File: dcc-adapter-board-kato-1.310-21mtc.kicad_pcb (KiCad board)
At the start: 2 copper layers, 59.5 x 16 mm, 25 parts

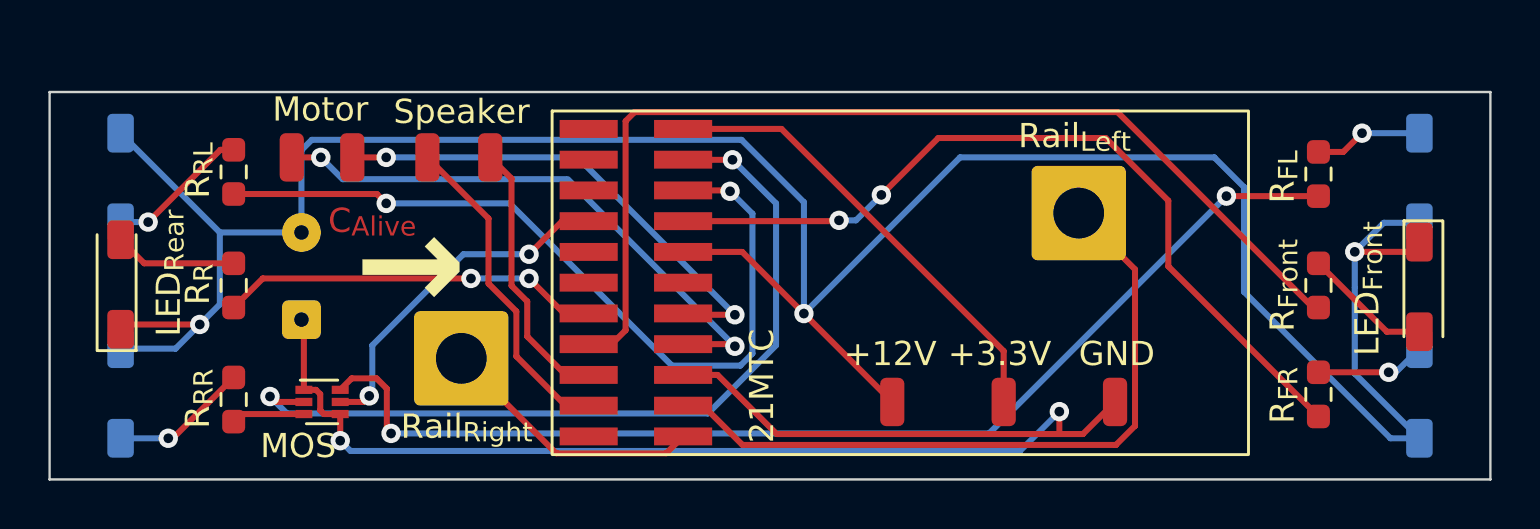
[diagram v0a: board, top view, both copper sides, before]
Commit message: 試作1号　フィードバック
ねじ穴位置修正
プラス表記
銅層の文字をシルクスクリーンに移動
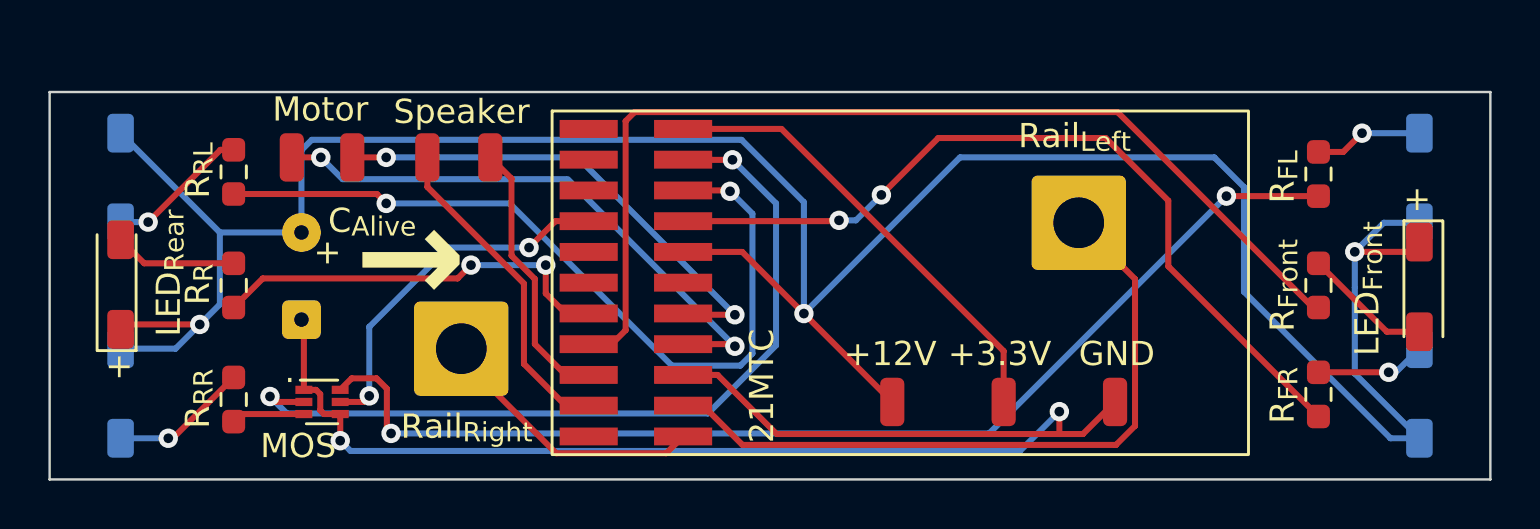
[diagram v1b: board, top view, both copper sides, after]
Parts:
- moved Rail_{Left}1 0.40 mm to (106.0, 30.8)
- moved Rail_{Right}1 0.40 mm to (80.5, 36.0)
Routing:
- net Net-(21MTC1-Rearlight): track 15.8 -> 16.9 mm
- net Net-(21MTC1-Aux_4): track 14.5 -> 15.0 mm
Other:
- board text added: "+"
- board text added: "."

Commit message: 改修
• 21MTC のピン配置がまちがっていた
• アライブキャパシター用端子をなくした
  • +12V・GND パッドを使うようにする
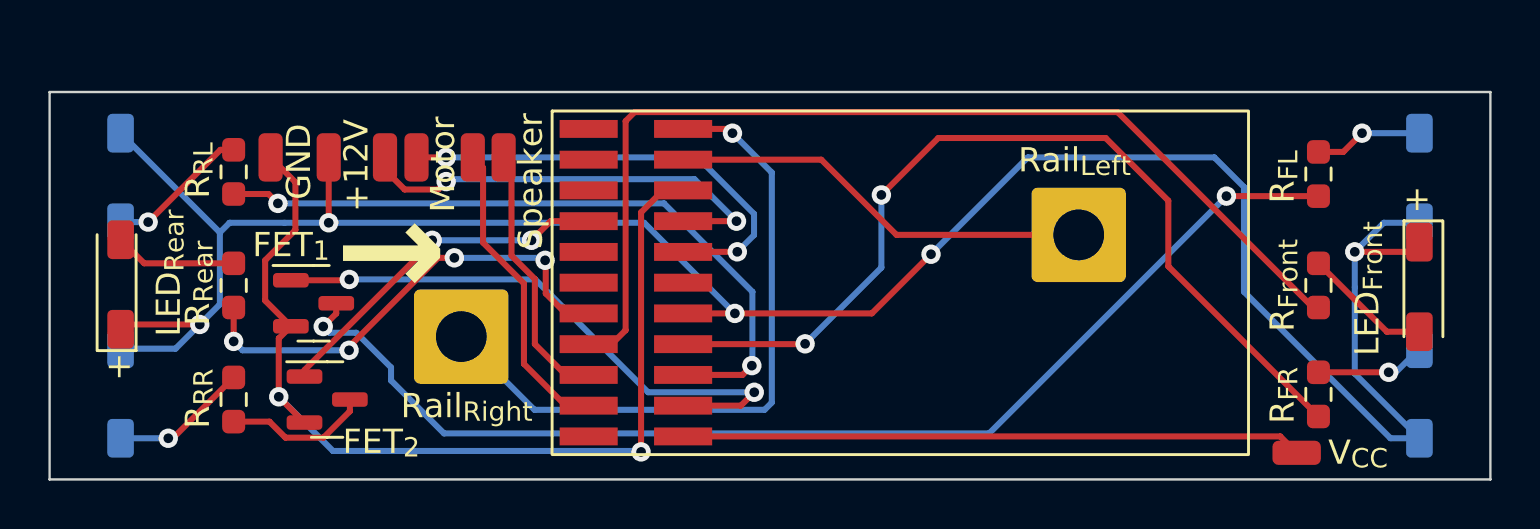
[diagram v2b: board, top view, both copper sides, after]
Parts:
- removed +3.3V1: J, Connector_Wire:SolderWirePad_1x01_SMD_1x2mm
- removed C_{Alive}1: C, Connector_Wire:SolderWire-0.1sqmm_1x02_P3.6mm_D0.4mm_OD1mm
- removed MOS1: NMOS, Package_TO_SOT_SMD:SOT-563
- added Q1: NMOSFET1, Package_TO_SOT_SMD:SOT-23, F.Cu at (74.4, 34.1)
- added Q2: NMOSFET2, Package_TO_SOT_SMD:SOT-23, F.Cu at (75.0, 38.1)
- added VCC1: J, Connector_Wire:SolderWirePad_1x01_SMD_1x2mm, F.Cu at (115.0, 40.3)
- moved GND1 36.3 mm to (72.6, 28.1)
- moved +12V1 25.4 mm to (75.0, 28.1)
- moved G1 8.26 mm to (87.6, 29.9)
- moved Motor_{1}1 3.85 mm to (77.3, 28.1)
- moved Motor_{2}1 2.65 mm to (78.7, 28.1)
- moved Speaker_{1}1 1.88 mm to (81.0, 28.1)
- moved Speaker_{2}1 0.55 mm to (82.2, 28.1)
- moved Rail_{Left}1 0.50 mm to (106.0, 31.3)
- moved Rail_{Right}1 0.50 mm to (80.5, 35.5)
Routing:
- net Net-(21MTC1-Rail_Right): track 11.5 -> 28.1 mm, vias 0 -> 1
- net GND: track 57.2 -> 40.9 mm
- net +12V: track 111.8 -> 97.9 mm, vias 3 -> 5
- net Net-(21MTC1-Rail_Left): track 29.0 -> 17.6 mm
- net Net-(21MTC1-Aux_3): track 34.3 -> 24.2 mm
- net Net-(21MTC1-Vcc): track 19.1 -> 25.6 mm
- net Net-(21MTC1-Motor_1): track 23.6 -> 18.5 mm
- net Net-(21MTC1-Aux_2): track 33.6 -> 29.2 mm
- net Net-(21MTC1-Aux_1): track 34.0 -> 37.9 mm
- net Net-(Q2-D): track 3.03 -> 6.01 mm
- net Net-(21MTC1-Rearlight): track 16.9 -> 19.6 mm, vias 2 -> 4
- net Net-(Q1-D): track 46.6 -> 48.5 mm
- net Net-(21MTC1-Motor_2): track 20.7 -> 19.0 mm
- net Net-(Speaker_{1}1-Pin_1): track 13.6 -> 12.8 mm
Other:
- board text added: "FET_{1}"
- board text added: "FET_{2}"
- board text added: "K 1-310 21MTC Adaptor Board ver. 2 2023.05.18 岡本和樹"
- board text added: "R_{Rear}"
- board text added: "V_{CC}"
- board text removed: "+3.3V"
- board text removed: "."
- board text removed: "21MTC"
- board text removed: "C_{Alive}"
- board text removed: "K 1-310 21MTC Adaptor Board ver. 1 2023.04.17 岡本和樹"
- board text removed: "MOS"
- board text removed: "R_{R}"

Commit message: v2 フィードバック
• MOSFET のゲートの前段に抵抗を追加
• ねじ穴の位置を 0.5mm 外側に移動
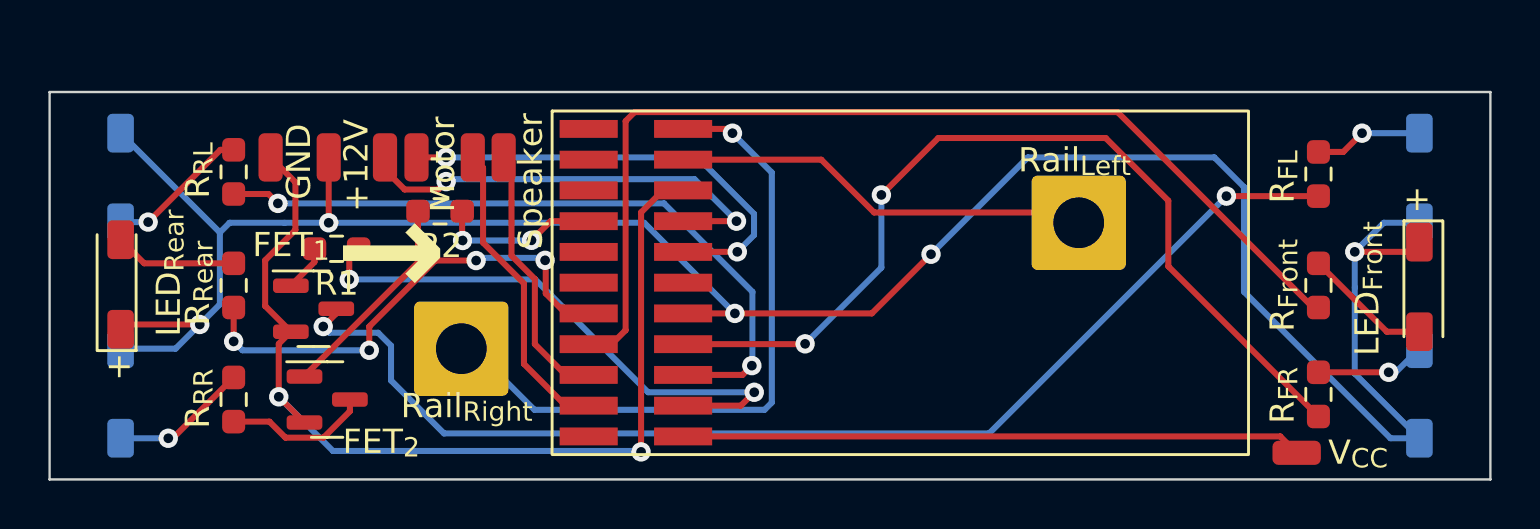
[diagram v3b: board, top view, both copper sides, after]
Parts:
- added R1: 1kΩ, Resistor_SMD:R_0603_1608Metric_Pad0.98x0.95mm_HandSolder, F.Cu at (75.3, 31.9)
- added R2: 1kΩ, Resistor_SMD:R_0603_1608Metric_Pad0.98x0.95mm_HandSolder, F.Cu at (79.6, 30.3)
- moved Rail_{Left}1 0.50 mm to (106.0, 30.8)
- moved Rail_{Right}1 0.50 mm to (80.5, 36.0)
- moved Q1 0.23 mm to (74.4, 34.4)
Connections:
- Q1 pad 1: Net-(21MTC1-Aux_3) -> Net-(Q1-G)
- Q2 pad 1: Net-(21MTC1-Aux_4) -> Net-(Q2-G)
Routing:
- net Net-(Q2-G): track 0.00 -> 8.77 mm
- net Net-(21MTC1-Aux_4): track 14.6 -> 6.75 mm
- net Net-(Q1-G): track 0.00 -> 1.93 mm
- net Net-(21MTC1-Aux_3): track 24.2 -> 23.3 mm
